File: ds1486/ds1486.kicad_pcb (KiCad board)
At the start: 2 copper layers, 15 parts, among them J2 DBG1-16, J3 DBG17-32, J4 DS1-16, J5 DS17-32, U1 RP2040, U2 FXMA108, U3 AMS1117-3.3, U4 FXMA108, U5 FXMA108, Y2 E3SB12E00004EE

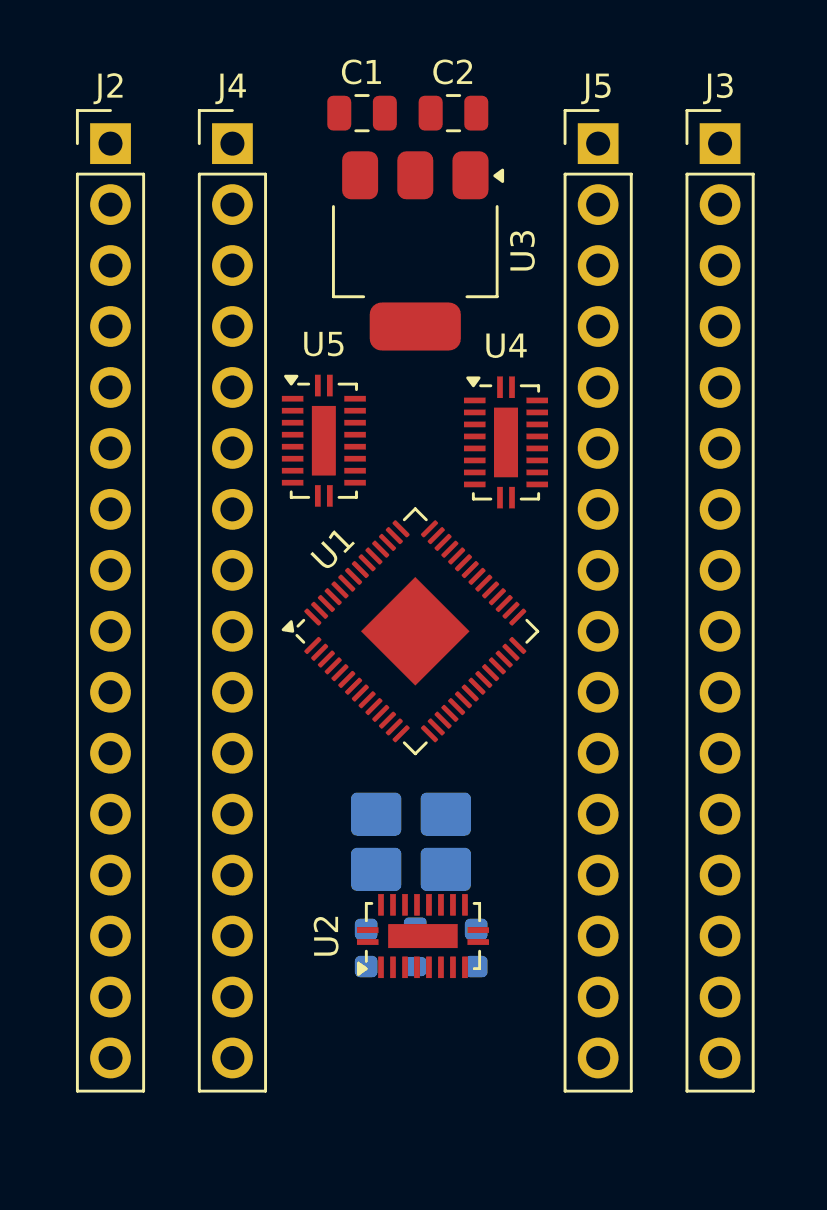
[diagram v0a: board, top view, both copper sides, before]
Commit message: PCB without RTC and battery.
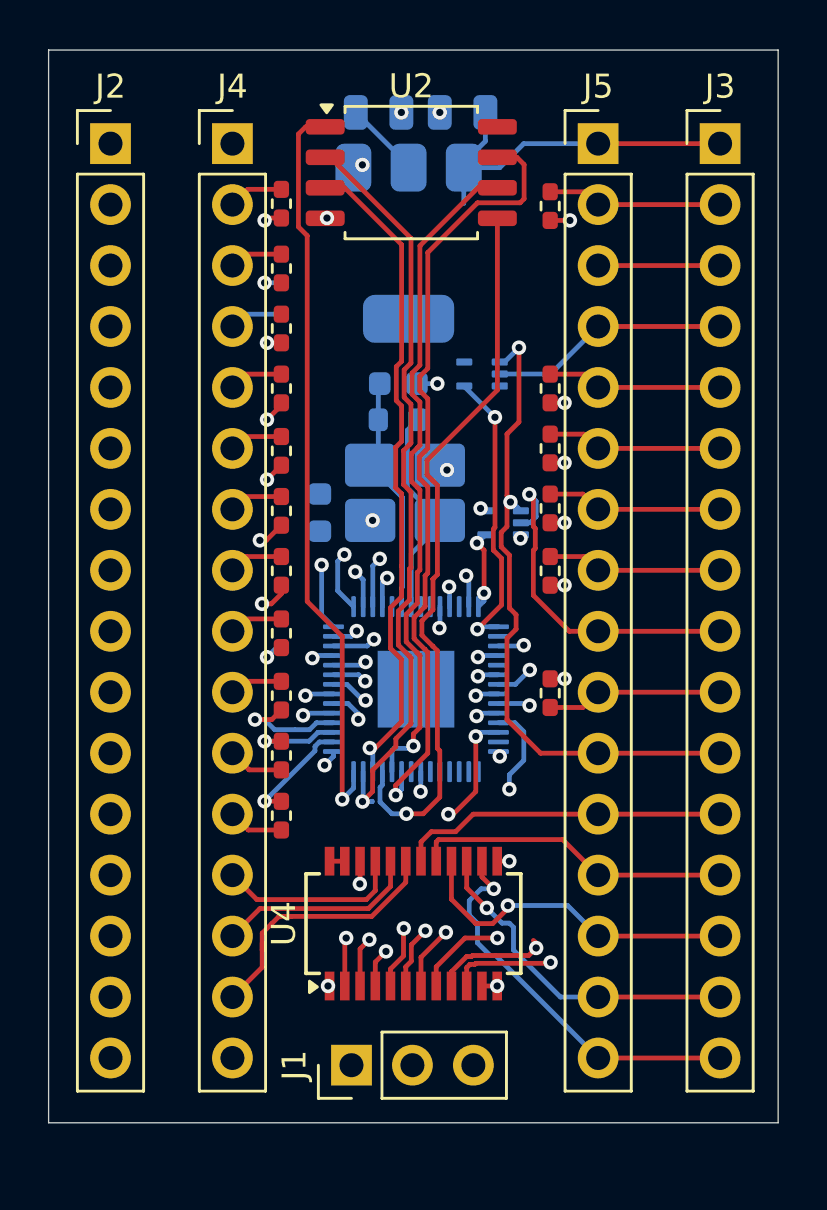
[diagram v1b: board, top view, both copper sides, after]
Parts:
- added J1: DBG, Connector_PinHeader_2.54mm:PinHeader_1x03_P2.54mm_Vertical, F.Cu at (116.7, 101.9)
- added R10: R, Resistor_SMD:R_0402_1005Metric_Pad0.72x0.64mm_HandSolder, F.Cu at (113.8, 76.3)
- added R11: R, Resistor_SMD:R_0402_1005Metric_Pad0.72x0.64mm_HandSolder, F.Cu at (125.0, 66.1)
- added R12: R, Resistor_SMD:R_0402_1005Metric_Pad0.72x0.64mm_HandSolder, F.Cu at (113.8, 68.7)
- added R13: R, Resistor_SMD:R_0402_1005Metric_Pad0.72x0.64mm_HandSolder, F.Cu at (125.0, 73.7)
- added R14: R, Resistor_SMD:R_0402_1005Metric_Pad0.72x0.64mm_HandSolder, F.Cu at (113.8, 71.2)
- added R15: R, Resistor_SMD:R_0402_1005Metric_Pad0.72x0.64mm_HandSolder, F.Cu at (125.0, 81.3)
- added R16: R, Resistor_SMD:R_0402_1005Metric_Pad0.72x0.64mm_HandSolder, F.Cu at (125.0, 86.4)
- added R17: R, Resistor_SMD:R_0402_1005Metric_Pad0.72x0.64mm_HandSolder, F.Cu at (125.0, 78.7)
- added R18: R, Resistor_SMD:R_0402_1005Metric_Pad0.72x0.64mm_HandSolder, F.Cu at (125.0, 76.2)
- added R19: R, Resistor_SMD:R_0402_1005Metric_Pad0.72x0.64mm_HandSolder, F.Cu at (113.8, 66.0)
- added R2: R, Resistor_SMD:R_0402_1005Metric_Pad0.72x0.64mm_HandSolder, F.Cu at (113.8, 91.5)
- added R4: R, Resistor_SMD:R_0402_1005Metric_Pad0.72x0.64mm_HandSolder, F.Cu at (113.8, 89.0)
- added R5: R, Resistor_SMD:R_0402_1005Metric_Pad0.72x0.64mm_HandSolder, F.Cu at (113.8, 83.9)
- added R6: R, Resistor_SMD:R_0402_1005Metric_Pad0.72x0.64mm_HandSolder, F.Cu at (113.8, 86.5)
- added R7: R, Resistor_SMD:R_0402_1005Metric_Pad0.72x0.64mm_HandSolder, F.Cu at (113.8, 78.8)
- added R8: R, Resistor_SMD:R_0402_1005Metric_Pad0.72x0.64mm_HandSolder, F.Cu at (113.8, 81.3)
- added R9: R, Resistor_SMD:R_0402_1005Metric_Pad0.72x0.64mm_HandSolder, F.Cu at (113.8, 73.7)
- added U7: SN74LVC1G00DRL, Package_TO_SOT_SMD:Texas_R-PDSO-N5_DRL-5, B.Cu at (123.0, 79.3)
- C1, C2, U1, U3: moved to B.Cu
- U2: value FXMA108 -> W25X20CLSNIG; footprint Package_DFN_QFN:WQFN-20-1EP_2.5x4.5mm_P0.5mm_EP1x2.9mm -> Package_SO:SOIC-8_5.3x5.3mm_P1.27mm
- U4: value FXMA108 -> SN74LVC8T245; footprint Package_DFN_QFN:WQFN-20-1EP_2.5x4.5mm_P0.5mm_EP1x2.9mm -> Package_SO:SSOP-24_3.9x8.7mm_P0.635mm
- U5: value FXMA108 -> SN74LVC1G00DRL; footprint Package_DFN_QFN:WQFN-20-1EP_2.5x4.5mm_P0.5mm_EP1x2.9mm -> Package_TO_SOT_SMD:Texas_R-PDSO-N5_DRL-5; moved to B.Cu
- moved U2 31.8 mm to (119.2, 64.7), turned to 0 degrees
- moved C3 23.6 mm to (118.7, 73.5), turned to 0 degrees
- moved R1 22.0 mm to (118.7, 75.0), turned to 0 degrees
- moved U4 20.4 mm to (119.3, 96.0), turned to 90 degrees
- moved C4 19.3 mm to (115.4, 78.9), turned to 90 degrees
- moved Y2 14.5 mm to (119.0, 78.0), turned to 0 degrees
- moved U5 7.15 mm to (122.2, 73.1), turned to 180 degrees
- moved C1 4.19 mm to (121.3, 62.2), turned to 180 degrees
- moved C2 3.12 mm to (117.8, 62.2)
- moved U1 2.41 mm to (119.4, 86.2), turned to 0 degrees
- moved U3 0.43 mm to (119.1, 67.7)
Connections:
- J3 pad 12: /DQ6 -> /DQ7
- J5 pad 12: /DQ6 -> /DQ7
- U1 pad 11: unconnected-(U1-GPIO8-Pad11) -> /AC12
- U1 pad 12: unconnected-(U1-GPIO9-Pad12) -> /AC14
- U1 pad 13: unconnected-(U1-GPIO10-Pad13) -> /AC16
- U1 pad 14: unconnected-(U1-GPIO11-Pad14) -> /AC15
- U1 pad 15: unconnected-(U1-GPIO12-Pad15) -> /AC13
- U1 pad 16: unconnected-(U1-GPIO13-Pad16) -> /AC8
- U1 pad 17: unconnected-(U1-GPIO14-Pad17) -> /AC9
- U1 pad 18: unconnected-(U1-GPIO15-Pad18) -> /AC11
- U1 pad 2: unconnected-(U1-GPIO0-Pad2) -> /AC0
- U1 pad 24: unconnected-(U1-SWCLK-Pad24) -> /SWCLK
- U1 pad 25: unconnected-(U1-SWD-Pad25) -> /SWD
- U1 pad 27: unconnected-(U1-GPIO16-Pad27) -> /AC10
- U1 pad 28: unconnected-(U1-GPIO17-Pad28) -> /CE_OE
- U1 pad 29: unconnected-(U1-GPIO18-Pad29) -> /CE_WE
- U1 pad 3: unconnected-(U1-GPIO1-Pad3) -> /AC1
- U1 pad 31: unconnected-(U1-GPIO20-Pad31) -> /DQC0
- U1 pad 32: unconnected-(U1-GPIO21-Pad32) -> /DQC1
- U1 pad 34: unconnected-(U1-GPIO22-Pad34) -> /DQC2
- U1 pad 35: unconnected-(U1-GPIO23-Pad35) -> /DQC3
- U1 pad 36: unconnected-(U1-GPIO24-Pad36) -> /DQC4
- U1 pad 37: unconnected-(U1-GPIO25-Pad37) -> /DQC5
- U1 pad 38: unconnected-(U1-GPIO26_ADC0-Pad38) -> /DQC6
- U1 pad 39: unconnected-(U1-GPIO27_ADC1-Pad39) -> /DQC7
- U1 pad 4: unconnected-(U1-GPIO2-Pad4) -> /AC2
- U1 pad 40: unconnected-(U1-GPIO28_ADC2-Pad40) -> /D_DIR
- U1 pad 5: unconnected-(U1-GPIO3-Pad5) -> /AC3
- U1 pad 51: unconnected-(U1-QSPI_SD3-Pad51) -> /QSPI_SD3
- U1 pad 52: unconnected-(U1-QSPI_SCLK-Pad52) -> /QSPI_SCLK
- U1 pad 53: unconnected-(U1-QSPI_SD0-Pad53) -> /QSPI_SD0
- U1 pad 54: unconnected-(U1-QSPI_SD2-Pad54) -> /QSPI_SD2
- U1 pad 55: unconnected-(U1-QSPI_SD1-Pad55) -> /QSPI_SD1
- U1 pad 56: unconnected-(U1-QSPI_SS-Pad56) -> /QSPI_SS
- U1 pad 57: unconnected-(U1-GND-Pad57) -> GND
- U1 pad 6: unconnected-(U1-GPIO4-Pad6) -> /AC4
- U1 pad 7: unconnected-(U1-GPIO5-Pad7) -> /AC5
- U1 pad 8: unconnected-(U1-GPIO6-Pad8) -> /AC6
- U1 pad 9: unconnected-(U1-GPIO7-Pad9) -> /AC7
- U2 pad 1: unconnected-(U2-VCCA-Pad1) -> /QSPI_SS
- U2 pad 2: unconnected-(U2-A0-Pad2) -> /QSPI_SD1
- U2 pad 3: unconnected-(U2-A1-Pad3) -> /QSPI_SD2
- U2 pad 4: unconnected-(U2-A2-Pad4) -> GND
- U2 pad 5: unconnected-(U2-A3-Pad5) -> /QSPI_SD0
- U2 pad 6: unconnected-(U2-A4-Pad6) -> /QSPI_SCLK
- U2 pad 7: unconnected-(U2-A5-Pad7) -> /QSPI_SD3
- U2 pad 8: unconnected-(U2-A6-Pad8) -> +3V3
- U4 pad 1: unconnected-(U4-VCCA-Pad1) -> +3V3
- U4 pad 10: unconnected-(U4-GND-Pad10) -> /DQC3
- U4 pad 11: unconnected-(U4-~{OE}-Pad11) -> GND
- U4 pad 12: unconnected-(U4-B7-Pad12) -> GND
- U4 pad 13: unconnected-(U4-B6-Pad13) -> GND
- U4 pad 14: unconnected-(U4-B5-Pad14) -> /DQ3
- U4 pad 15: unconnected-(U4-B4-Pad15) -> /DQ4
- U4 pad 16: unconnected-(U4-B3-Pad16) -> /DQ5
- U4 pad 17: unconnected-(U4-B2-Pad17) -> /DQ6
- U4 pad 18: unconnected-(U4-B1-Pad18) -> /DQ7
- U4 pad 19: unconnected-(U4-B0-Pad19) -> /DQ2
- U4 pad 2: unconnected-(U4-A0-Pad2) -> /D_DIR
- U4 pad 20: unconnected-(U4-VCCB-Pad20) -> /DQ1
- U4 pad 21: unconnected-(U4-NC-Pad21) -> /DQ0
- U4 pad 3: unconnected-(U4-A1-Pad3) -> /DQC0
- U4 pad 4: unconnected-(U4-A2-Pad4) -> /DQC1
- U4 pad 5: unconnected-(U4-A3-Pad5) -> /DQC2
- U4 pad 6: unconnected-(U4-A4-Pad6) -> /DQC7
- U4 pad 7: unconnected-(U4-A5-Pad7) -> /DQC6
- U4 pad 8: unconnected-(U4-A6-Pad8) -> /DQC5
- U4 pad 9: unconnected-(U4-A7-Pad9) -> /DQC4
- U5 pad 1: unconnected-(U5-VCCA-Pad1) -> /CE_
- U5 pad 2: unconnected-(U5-A0-Pad2) -> /WE_
- U5 pad 3: unconnected-(U5-A1-Pad3) -> GND
- U5 pad 4: unconnected-(U5-A2-Pad4) -> /CE_WE
- U5 pad 5: unconnected-(U5-A3-Pad5) -> +3V3
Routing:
- net /QSPI_SD3: track 0.00 -> 32.9 mm, vias 0 -> 1
- net /QSPI_SD1: track 0.00 -> 31.9 mm, vias 0 -> 1
- net /QSPI_SS: track 0.00 -> 31.1 mm, vias 0 -> 1
- net /QSPI_SD0: track 0.00 -> 30.4 mm, vias 0 -> 1
- net /QSPI_SCLK: track 0.00 -> 28.1 mm, vias 0 -> 1
- net /QSPI_SD2: track 0.00 -> 27.6 mm, vias 0 -> 1
- net /CE_: track 0.00 -> 27.4 mm, vias 0 -> 2
- net /AC15: track 0.00 -> 27.1 mm, vias 0 -> 2
- net /DQC0: track 0.00 -> 22.6 mm, vias 0 -> 2
- net /AC16: track 0.00 -> 22.1 mm, vias 0 -> 2
- net /SWCLK: track 0.00 -> 21.6 mm, vias 0 -> 1
- net /AC14: track 0.00 -> 21.4 mm, vias 0 -> 2
- net /DQC4: track 0.00 -> 19.8 mm, vias 0 -> 2
- net /DQC3: track 0.00 -> 18.7 mm, vias 0 -> 2
- net /AC13: track 0.00 -> 18.0 mm, vias 0 -> 2
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- added copper zone on In2.Cu, net GND
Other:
- board outline added: 30.4 x 44.7 mm
- copper layers 2 -> 4

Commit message: Add RTC.
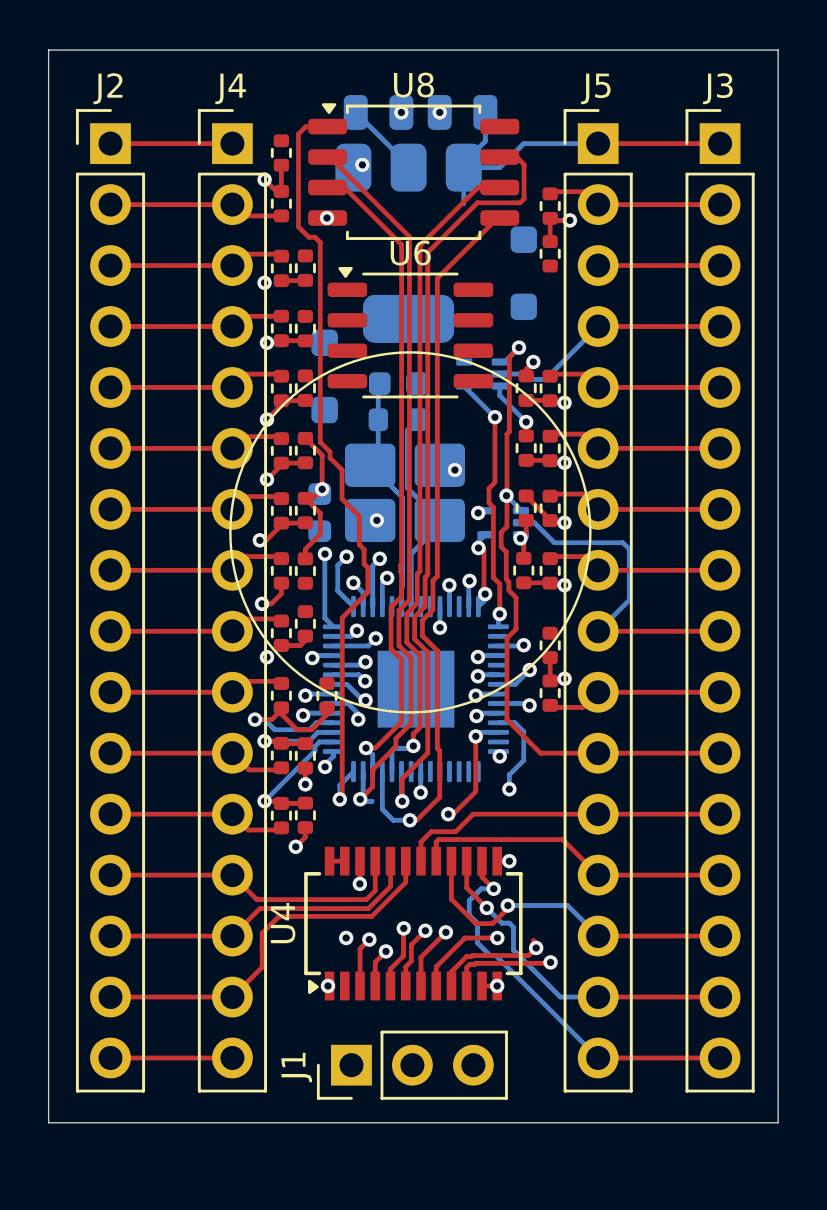
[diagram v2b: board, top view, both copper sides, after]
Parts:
- removed U2: W25X20CLSNIG, Package_SO:SOIC-8_5.3x5.3mm_P1.27mm
- added D1: BZT52C6V8-7-F, Diode_SMD:D_SOD-123F, B.Cu at (123.9, 68.9)
- added D2: BZT52C6V8-7-F, Diode_SMD:D_SOD-123F, B.Cu at (115.6, 73.2)
- added R20: 3k, Resistor_SMD:R_0402_1005Metric, F.Cu at (114.8, 89.0)
- added R21: 3k, Resistor_SMD:R_0402_1005Metric, F.Cu at (115.7, 86.5)
- added R22: 3k, Resistor_SMD:R_0402_1005Metric, F.Cu at (114.8, 83.5)
- added R23: 3k, Resistor_SMD:R_0402_1005Metric, F.Cu at (114.8, 81.3)
- added R24: 3k, Resistor_SMD:R_0402_1005Metric, F.Cu at (114.8, 78.8)
- added R25: 3k, Resistor_SMD:R_0402_1005Metric, F.Cu at (114.8, 76.3)
- added R26: 3k, Resistor_SMD:R_0402_1005Metric, F.Cu at (114.8, 73.7)
- added R27: 3k, Resistor_SMD:R_0402_1005Metric, F.Cu at (124.0, 76.2)
- added R28: 3k, Resistor_SMD:R_0402_1005Metric, F.Cu at (124.0, 78.7)
- added R29: 3k, Resistor_SMD:R_0402_1005Metric, F.Cu at (125.0, 84.4)
- added R3: 3k, Resistor_SMD:R_0402_1005Metric, F.Cu at (114.8, 91.5)
- added R30: 3k, Resistor_SMD:R_0402_1005Metric, F.Cu at (123.9, 81.3)
- added R31: 3k, Resistor_SMD:R_0402_1005Metric, F.Cu at (114.8, 71.2)
- added R32: 3k, Resistor_SMD:R_0402_1005Metric, F.Cu at (124.0, 73.7)
- added R33: 3k, Resistor_SMD:R_0402_1005Metric, F.Cu at (114.8, 68.7)
- added R34: 3k, Resistor_SMD:R_0402_1005Metric, F.Cu at (125.0, 68.1)
- added R35: 3k, Resistor_SMD:R_0402_1005Metric, F.Cu at (113.8, 63.9)
- added U6: YSN8010SJ, Package_SO:SOP-8_3.9x4.9mm_P1.27mm, F.Cu at (119.2, 71.5)
- added U8: W25Q16JVSS, Package_SO:SOIC-8_5.3x5.3mm_P1.27mm, F.Cu at (119.3, 64.7)
- R10, R11, R12, R13, R14, R15, R16, R17, R18, R19, R2, R4, R5, R6, R7, R8, R9: value R -> 1k; footprint Resistor_SMD:R_0402_1005Metric_Pad0.72x0.64mm_HandSolder -> Resistor_SMD:R_0402_1005Metric
- turned R19 to 90 degrees
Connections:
- U1 pad 30: unconnected-(U1-GPIO19-Pad30) -> /SCL
- U1 pad 40: /D_DIR -> GND
- U1 pad 41: unconnected-(U1-GPIO29_ADC3-Pad41) -> /SDA
- U4 pad 2: /D_DIR -> unconnected-(U4-DIR-Pad2)
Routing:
- net GND: track 4.28 -> 34.0 mm, vias 11 -> 18
- net /SWD: track 0.84 -> 27.5 mm
- net /D_DIR: track 13.8 -> 0.00 mm, vias 3 -> 0
- net /A12: track 2.25 -> 8.03 mm
- net /DQ2: track 11.2 -> 16.3 mm
- net /INTB_: track 0.00 -> 5.08 mm
- net /DQ1: track 8.50 -> 13.6 mm
- net /A7: track 2.27 -> 7.35 mm
- net /A6: track 2.95 -> 8.03 mm
- net /A5: track 3.02 -> 8.10 mm
- net /A4: track 2.28 -> 7.36 mm
- net /A3: track 2.98 -> 8.06 mm
- net /A2: track 2.87 -> 7.95 mm
- net /A1: track 2.33 -> 7.41 mm
- net /A0: track 2.31 -> 7.39 mm
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
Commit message: Add battery and narrow pin header.
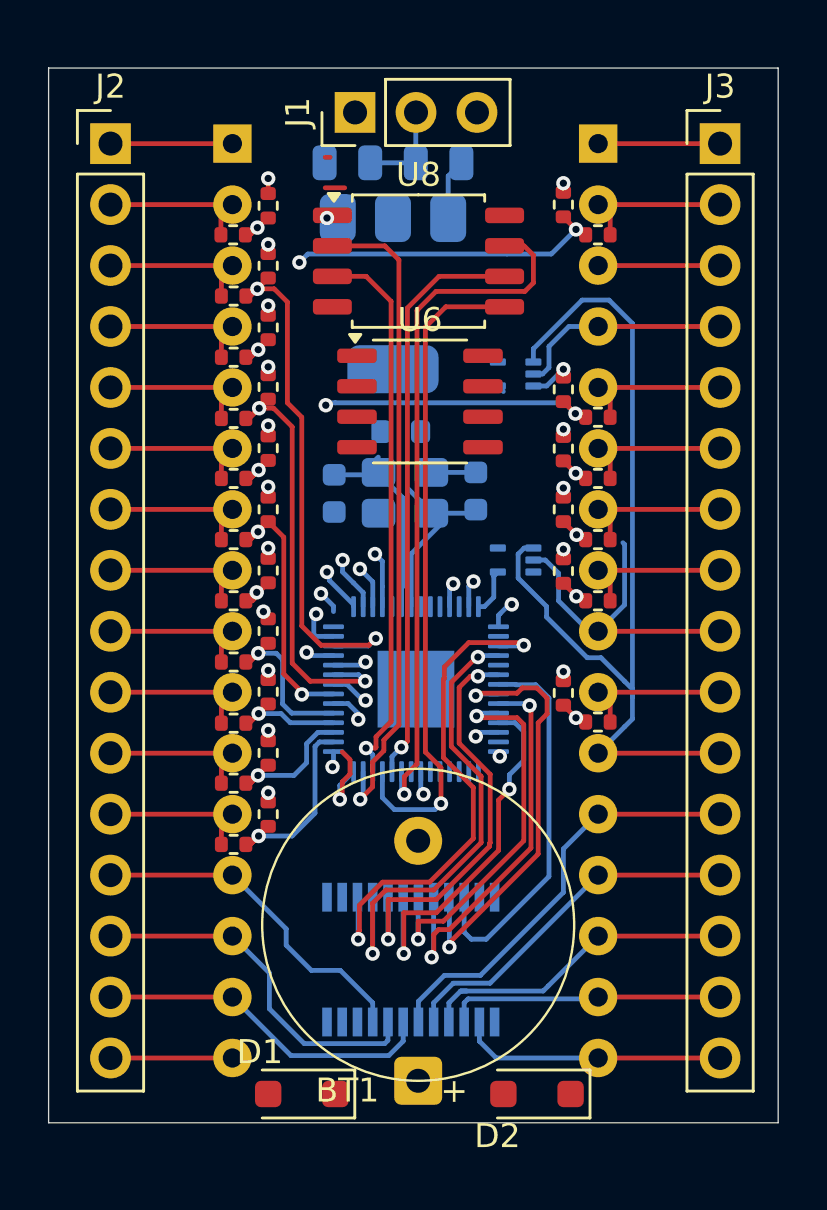
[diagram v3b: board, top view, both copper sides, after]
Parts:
- added BT1: CR1225 H2, Kicad_Personal:CR1225_H2, F.Cu at (119.5, 96.0)
- D1, D2: moved to F.Cu
- J4, J5: footprint Connector_PinHeader_2.54mm:PinHeader_1x16_P2.54mm_Vertical -> Kicad_Personal:PinHeader_1x16_P2.54mm_Vertical_DIP_Diameter_Flipside
- U4: moved to B.Cu
- Y2: footprint Crystal:Crystal_SMD_3225-4Pin_3.2x2.5mm_HandSoldering -> Crystal:Crystal_SMD_3225-4Pin_3.2x2.5mm
- moved J1 39.7 mm to (116.9, 62.2)
- moved D1 35.4 mm to (114.7, 103.1), turned to 180 degrees
- moved D2 31.2 mm to (124.5, 103.1), turned to 180 degrees
- moved C4 6.56 mm to (121.9, 78.0)
- moved C3 5.30 mm to (116.0, 78.1), turned to -90 degrees
- moved U8 3.71 mm to (119.5, 68.4)
- moved U6 2.78 mm to (119.6, 74.2)
- moved C2 2.47 mm to (116.5, 64.3)
- moved R21 2.46 mm to (113.2, 86.3)
- moved R19 2.39 mm to (111.8, 67.3), turned to 0 degrees
- moved R17 2.38 mm to (127.0, 80.0), turned to 180 degrees
- moved R15 2.35 mm to (127.0, 82.5), turned to 180 degrees
- moved R18 2.35 mm to (127.0, 77.5), turned to 180 degrees
- moved R8 2.35 mm to (111.8, 82.5), turned to 0 degrees
- moved R9 2.35 mm to (111.8, 75.0), turned to 0 degrees
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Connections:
- U6 pad 3: unconnected-(U6-FOUT-Pad3) -> Net-(U6-FOUT)
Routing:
- net /QSPI_SS: track 32.2 -> 4.70 mm
- net /SWD: track 27.5 -> 1.02 mm
- net /SWCLK: track 21.6 -> 0.00 mm, vias 1 -> 0
- net GND: track 34.0 -> 22.7 mm, vias 18 -> 19
- net /CE_: track 27.6 -> 38.5 mm, vias 2 -> 0
- net /CE_WE: track 10.9 -> 1.54 mm, vias 2 -> 1
- net +5V: track 15.9 -> 7.61 mm
- net /AC10: track 9.89 -> 15.5 mm
- net /DQ3: track 16.6 -> 11.1 mm, vias 1 -> 0
- net /AC16: track 25.5 -> 20.5 mm
- net /QSPI_SD2: track 27.5 -> 23.2 mm
- net /DQ7: track 13.7 -> 17.7 mm
- net /QSPI_SD1: track 31.3 -> 27.5 mm
- net +3V3: track 6.89 -> 3.26 mm, vias 6 -> 4
- net /QSPI_SD3: track 32.6 -> 29.2 mm
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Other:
- board size 30.4 x 44.7 mm -> 30.4 x 43.9 mm

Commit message: Fully routed.
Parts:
- added C10: 100n, Capacitor_SMD:C_0603_1608Metric, B.Cu at (121.5, 84.2)
- added C11: 1u, Capacitor_SMD:C_0603_1608Metric, B.Cu at (119.0, 87.2)
- added C12: 1u, Capacitor_SMD:C_0603_1608Metric, B.Cu at (117.3, 90.1)
- added C13: 100n, Capacitor_SMD:C_0603_1608Metric, B.Cu at (117.5, 82.6)
- added C14: 100n, Capacitor_SMD:C_0603_1608Metric, B.Cu at (120.4, 89.6)
- added C15: 100n, Capacitor_SMD:C_0603_1608Metric, B.Cu at (114.5, 95.7)
- added C16: 100n, Capacitor_SMD:C_0603_1608Metric, B.Cu at (114.5, 99.7)
- added C17: 100n, Capacitor_SMD:C_0603_1608Metric, B.Cu at (123.4, 64.5)
- added C5: 100n, Capacitor_SMD:C_0603_1608Metric, B.Cu at (118.8, 89.6)
- added C6: 100n, Capacitor_SMD:C_0603_1608Metric, B.Cu at (115.7, 89.6)
- added C7: 100n, Capacitor_SMD:C_0603_1608Metric, B.Cu at (118.3, 84.9)
- added C8: 100n, Capacitor_SMD:C_0603_1608Metric, B.Cu at (119.1, 82.6)
- added C9: 100n, Capacitor_SMD:C_0603_1608Metric, B.Cu at (122.9, 89.6)
- added R36: 10k, Resistor_SMD:R_0402_1005Metric, F.Cu at (117.0, 79.7)
- added R37: 4k7, Resistor_SMD:R_0603_1608Metric, B.Cu at (121.7, 79.6)
- added R38: 4k7, Resistor_SMD:R_0603_1608Metric, B.Cu at (119.2, 77.8)
- C3, C4, R1, U1, U3, U5, U7, Y2: moved to F.Cu
- U6, U8: moved to B.Cu
- moved C3 5.89 mm to (121.8, 77.4)
- moved C4 5.83 mm to (116.1, 77.4)
- moved C1 3.85 mm to (116.5, 64.5), turned to 0 degrees
- moved C2 3.45 mm to (120.0, 64.5), turned to 180 degrees
- moved U1 1.00 mm to (119.2, 85.2), turned to 180 degrees
- moved U4 0.78 mm to (120.0, 97.7)
- moved U7 0.65 mm to (123.6, 80.2)
- moved Y2 0.65 mm to (119.0, 77.4), turned to 180 degrees
- moved R1 0.60 mm to (118.8, 74.9), turned to 180 degrees
- moved D1 0.15 mm to (114.7, 103.0)
- moved D2 0.15 mm to (124.5, 103.0)
- turned U6 to 180 degrees
- turned U8 to 180 degrees
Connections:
- U1 pad 11: /AC12 -> /DQC7
- U1 pad 12: /AC14 -> /SCL
- U1 pad 13: /AC16 -> /SDA
- U1 pad 14: /AC15 -> /CE_WE
- U1 pad 15: /AC13 -> /CE_OE
- U1 pad 16: /AC8 -> /AC10
- U1 pad 17: /AC9 -> /AC11
- U1 pad 18: /AC11 -> /AC9
- U1 pad 19: unconnected-(U1-TESTEN-Pad19) -> GND
- U1 pad 2: /AC0 -> /D_DIR
- U1 pad 23: Net-(U1-DVDD-Pad23) -> +1V1
- U1 pad 26: unconnected-(U1-RUN-Pad26) -> /RUN
- U1 pad 27: /AC10 -> /AC8
- U1 pad 28: /CE_OE -> /AC13
- U1 pad 29: /CE_WE -> /AC15
- U1 pad 3: /AC1 -> /DQC0
- U1 pad 30: /SCL -> /AC16
- U1 pad 31: /DQC0 -> /AC14
- U1 pad 32: /DQC1 -> /AC12
- U1 pad 34: /DQC2 -> /AC7
- U1 pad 35: /DQC3 -> /AC6
- U1 pad 36: /DQC4 -> /AC5
- U1 pad 37: /DQC5 -> /AC4
- U1 pad 38: /DQC6 -> /AC0
- U1 pad 39: /DQC7 -> /AC1
- U1 pad 4: /AC2 -> /DQC1
- U1 pad 40: GND -> /AC2
- U1 pad 41: /SDA -> /AC3
- U1 pad 43: unconnected-(U1-ADC_AVDD-Pad43) -> +3V3
- U1 pad 44: unconnected-(U1-VREG_IN-Pad44) -> +3V3
- U1 pad 45: unconnected-(U1-VREG_VOUT-Pad45) -> +1V1
- U1 pad 48: unconnected-(U1-USB_VDD-Pad48) -> +3V3
- U1 pad 5: /AC3 -> /DQC2
- U1 pad 50: Net-(U1-DVDD-Pad23) -> +1V1
- U1 pad 6: /AC4 -> /DQC3
- U1 pad 7: /AC5 -> /DQC4
- U1 pad 8: /AC6 -> /DQC5
- U1 pad 9: /AC7 -> /DQC6
- U4 pad 2: unconnected-(U4-DIR-Pad2) -> /D_DIR
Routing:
- net +5V: track 7.61 -> 72.8 mm, vias 0 -> 3
- net +3V3: track 3.26 -> 67.3 mm, vias 4 -> 17
- net /VRTC: track 0.00 -> 51.7 mm, vias 0 -> 1
- net /SWD: track 1.02 -> 31.6 mm
- net /QSPI_SS: track 4.70 -> 33.0 mm
- net /SWCLK: track 0.00 -> 24.9 mm, vias 0 -> 1
- net +1V1: track 0.00 -> 18.9 mm, vias 0 -> 3
- net /AC8: track 17.6 -> 35.8 mm
- net /CE_: track 38.5 -> 23.5 mm
- net /D_DIR: track 0.00 -> 14.5 mm, vias 0 -> 1
- net /SCL: track 0.00 -> 13.8 mm, vias 0 -> 1
- net /AC13: track 21.1 -> 34.1 mm, vias 3 -> 0
- net /SDA: track 0.00 -> 10.7 mm, vias 0 -> 1
- net /CE_WE: track 1.54 -> 11.7 mm, vias 1 -> 0
- net GND: track 22.7 -> 31.8 mm, vias 19 -> 39
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- added copper zone on In1.Cu, net +3V3
